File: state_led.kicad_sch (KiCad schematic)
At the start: 5 parts

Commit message: routing done
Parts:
- removed D1, D2, D3, D4, D5: White, LED_SMD:LED_0603_1608Metric, symbol Device:LED
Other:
- added sheet LED array x5 (led_x5.kicad_sch)
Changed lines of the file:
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@@
 (kicad_sch (version 20211123) (generator eeschema)
   (paper "A4")
-  (junction (at 106.68 109.855) (diameter 0) (color 0 0 0 0)
-  )
-  (junction (at 106.68 90.805) (diameter 0) (color 0 0 0 0)
-  )
-  (junction (at 106.68 103.505) (diameter 0) (color 0 0 0 0)
-  )
-  (junction (at 106.68 97.155) (diameter 0) (color 0 0 0 0)
-  )
-  (wire (pts (xy 106.68 109.855) (xy 106.68 103.505))
+  (wire (pts (xy 111.125 83.185) (xy 114.3 83.185))
     (stroke (width 0) (type default) (color 0 0 0 0))
   )
-  (wire (pts (xy 106.68 97.155) (xy 106.68 90.805))
+  (wire (pts (xy 111.125 88.9) (xy 114.3 88.9))
     (stroke (width 0) (type default) (color 0 0 0 0))
   )
-  (wire (pts (xy 106.68 90.805) (xy 106.68 84.455))
+  (wire (pts (xy 111.125 85.09) (xy 114.3 85.09))
     (stroke (width 0) (type default) (color 0 0 0 0))
   )
-  (wire (pts (xy 106.68 103.505) (xy 106.68 97.155))
+  (wire (pts (xy 111.125 81.28) (xy 114.3 81.28))
+    (stroke (width 0) (type default) (color 0 0 0 0))
+  )
+  (wire (pts (xy 111.125 86.995) (xy 114.3 86.995))
     (stroke (width 0) (type default) (color 0 0 0 0))
   )
   (hierarchical_label "STATE" (shape input) (at 114.3 76.2 180)
     (effects (font (size 1.27 1.27)) (justify right))
-  )
-  (symbol (lib_id "Device:LED") (at 110.49 97.155 180) (unit 1)
-    (in_bom yes) (on_board yes) (fields_autoplaced)
-    (property "Reference" "D3" (id 0) (at 112.0775 93.8332 0))
-    (property "Value" "White" (id 1) (at 113.7797 94.234 90)
-      (effects (font (size 1.27 1.27)) (justify right) hide)
-    )
-    (property "Footprint" "LED_SMD:LED_0603_1608Metric" (id 2) (at 110.49 97.155 0)
-      (effects (font (size 1.27 1.27)) hide)
-    )
-    (property "Datasheet" "https://datasheet.lcsc.com/lcsc/1809041711_Hubei-KENTO-Elec-C2290_C2290.pdf" (id 3) (at 110.49 97.155 0)
-      (effects (font (size 1.27 1.27)) hide)
-    )
-    (property "JLC" "C2290" (id 4) (at 110.49 97.155 90)
-      (effects (font (size 1.27 1.27)) hide)
-    )
-    (pin "1")
-    (pin "2")
-  )
-  (symbol (lib_id "Device:LED") (at 110.49 109.855 180) (unit 1)
-    (in_bom yes) (on_board yes) (fields_autoplaced)
-    (property "Reference" "D5" (id 0) (at 112.0775 106.5332 0))
-    (property "Value" "White" (id 1) (at 113.7797 106.934 90)
-      (effects (font (size 1.27 1.27)) (justify right) hide)
-    )
-    (property "Footprint" "LED_SMD:LED_0603_1608Metric" (id 2) (at 110.49 109.855 0)
-      (effects (font (size 1.27 1.27)) hide)
-    )
-    (property "Datasheet" "https://datasheet.lcsc.com/lcsc/1809041711_Hubei-KENTO-Elec-C2290_C2290.pdf" (id 3) (at 110.49 109.855 0)
-      (effects (font (size 1.27 1.27)) hide)
-    )
-    (property "JLC" "C2290" (id 4) (at 110.49 109.855 90)
-      (effects (font (size 1.27 1.27)) hide)
-    )
-    (pin "1")
-    (pin "2")
-  )
-  (symbol (lib_id "Device:LED") (at 110.49 84.455 180) (unit 1)
-    (in_bom yes) (on_board yes) (fields_autoplaced)
-    (property "Reference" "D1" (id 0) (at 112.0775 81.1332 0))
-    (property "Value" "White" (id 1) (at 113.7797 81.534 90)
-      (effects (font (size 1.27 1.27)) (justify right) hide)
-    )
-    (property "Footprint" "LED_SMD:LED_0603_1608Metric" (id 2) (at 110.49 84.455 0)
-      (effects (font (size 1.27 1.27)) hide)
-    )
-    (property "Datasheet" "https://datasheet.lcsc.com/lcsc/1809041711_Hubei-KENTO-Elec-C2290_C2290.pdf" (id 3) (at 110.49 84.455 0)
-      (effects (font (size 1.27 1.27)) hide)
-    )
-    (property "JLC" "C2290" (id 4) (at 110.49 84.455 90)
-      (effects (font (size 1.27 1.27)) hide)
-    )
-    (pin "1")
-    (pin "2")
-  )
-  (symbol (lib_id "power:VDD") (at 106.68 109.855 90) (unit 1)
-    (in_bom yes) (on_board yes) (fields_autoplaced)
-    (property "Reference" "#PWR021" (id 0) (at 110.49 109.855 0)
-      (effects (font (size 1.27 1.27)) hide)
-    )
-    (property "Value" "VDD" (id 1) (at 103.505 110.2888 90)
-      (effects (font (size 1.27 1.27)) (justify left))
-    )
-    (property "Footprint" "" (id 2) (at 106.68 109.855 0)
-      (effects (font (size 1.27 1.27)) hide)
-    )
-    (property "Datasheet" "" (id 3) (at 106.68 109.855 0)
-      (effects (font (size 1.27 1.27)) hide)
-    )
-    (pin "1")
-  )
-  (symbol (lib_id "Device:LED") (at 110.49 90.805 180) (unit 1)
-    (in_bom yes) (on_board yes) (fields_autoplaced)
-    (property "Reference" "D2" (id 0) (at 112.0775 87.4832 0))
-    (property "Value" "White" (id 1) (at 113.7797 87.884 90)
-      (effects (font (size 1.27 1.27)) (justify right) hide)
-    )
-    (property "Footprint" "LED_SMD:LED_0603_1608Metric" (id 2) (at 110.49 90.805 0)
-      (effects (font (size 1.27 1.27)) hide)
-    )
-    (property "Datasheet" "https://datasheet.lcsc.com/lcsc/1809041711_Hubei-KENTO-Elec-C2290_C2290.pdf" (id 3) (at 110.49 90.805 0)
-      (effects (font (size 1.27 1.27)) hide)
-    )
-    (property "JLC" "C2290" (id 4) (at 110.49 90.805 90)
-      (effects (font (size 1.27 1.27)) hide)
-    )
-    (pin "1")
-    (pin "2")
-  )
-  (symbol (lib_id "Device:LED") (at 110.49 103.505 180) (unit 1)
-    (in_bom yes) (on_board yes) (fields_autoplaced)
-    (property "Reference" "D4" (id 0) (at 112.0775 100.1832 0))
-    (property "Value" "White" (id 1) (at 113.7797 100.584 90)
-      (effects (font (size 1.27 1.27)) (justify right) hide)
-    )
-    (property "Footprint" "LED_SMD:LED_0603_1608Metric" (id 2) (at 110.49 103.505 0)
-      (effects (font (size 1.27 1.27)) hide)
-    )
-    (property "Datasheet" "https://datasheet.lcsc.com/lcsc/1809041711_Hubei-KENTO-Elec-C2290_C2290.pdf" (id 3) (at 110.49 103.505 0)
-      (effects (font (size 1.27 1.27)) hide)
-    )
-    (property "JLC" "C2290" (id 4) (at 110.49 103.505 90)
-      (effects (font (size 1.27 1.27)) hide)
-    )
-    (pin "1")
-    (pin "2")
   )
   (sheet (at 114.3 74.93) (size 12.7 40.005) (fields_autoplaced)
@@
       (effects (font (size 1.27 1.27)) (justify left top) hide)
     )
-    (pin "LED2" passive (at 114.3 90.805 180)
+    (pin "LED2" passive (at 114.3 83.185 180)
       (effects (font (size 1.27 1.27)) (justify left))
     )
-    (pin "LED1" passive (at 114.3 84.455 180)
+    (pin "LED1" passive (at 114.3 81.28 180)
       (effects (font (size 1.27 1.27)) (justify left))
     )
-    (pin "LED3" passive (at 114.3 97.155 180)
+    (pin "LED3" passive (at 114.3 85.09 180)
       (effects (font (size 1.27 1.27)) (justify left))
     )
@@
       (effects (font (size 1.27 1.27)) (justify left))
     )
-    (pin "LED4" passive (at 114.3 103.505 180)
+    (pin "LED4" passive (at 114.3 86.995 180)
       (effects (font (size 1.27 1.27)) (justify left))
     )
-    (pin "LED5" passive (at 114.3 109.855 180)
+    (pin "LED5" passive (at 114.3 88.9 180)
       (effects (font (size 1.27 1.27)) (justify left))
     )
   )
+  (sheet (at 93.98 80.01) (size 17.145 10.16) (fields_autoplaced)
+    (stroke (width 0.1524) (type solid) (color 0 0 0 0))
+    (fill (color 0 0 0 0.0000))
+    (property "Sheet name" "LED array x5" (id 0) (at 93.98 79.2984 0)
+      (effects (font (size 1.27 1.27)) (justify left bottom))
+    )
+    (property "Sheet file" "led_x5.kicad_sch" (id 1) (at 93.98 90.7546 0)
+      (effects (font (size 1.27 1.27)) (justify left top) hide)
+    )
+    (pin "LED3" passive (at 111.125 85.09 0)
+      (effects (font (size 1.27 1.27)) (justify right))
+    )
+    (pin "LED4" passive (at 111.125 86.995 0)
+      (effects (font (size 1.27 1.27)) (justify right))
+    )
+    (pin "LED1" passive (at 111.125 81.28 0)
+      (effects (font (size 1.27 1.27)) (justify right))
+    )
+    (pin "LED2" passive (at 111.125 83.185 0)
+      (effects (font (size 1.27 1.27)) (justify right))
+    )
+    (pin "LED5" passive (at 111.125 88.9 0)
+      (effects (font (size 1.27 1.27)) (justify right))
+    )
+  )

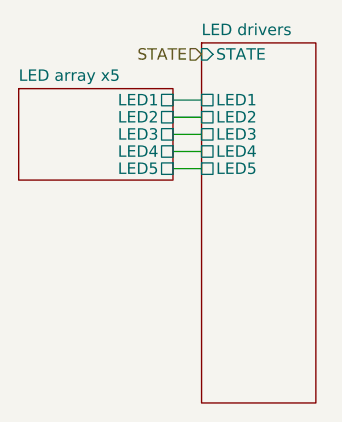
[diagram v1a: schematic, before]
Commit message: started fixing issues from V1
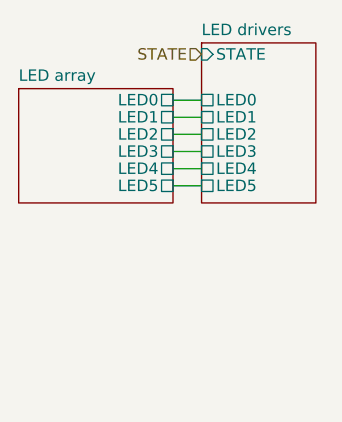
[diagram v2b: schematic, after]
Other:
- sheet LED array x5 renamed LED array
- sheet LED array ports: added LED0; removed none
- sheet LED drivers ports: added LED0; removed none
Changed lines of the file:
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@@
+    (stroke (width 0) (type default) (color 0 0 0 0))
+  )
+  (wire (pts (xy 111.125 90.805) (xy 114.3 90.805))
     (stroke (width 0) (type default) (color 0 0 0 0))
   )
@@
     (effects (font (size 1.27 1.27)) (justify right))
   )
-  (sheet (at 114.3 74.93) (size 12.7 40.005) (fields_autoplaced)
+  (sheet (at 114.3 74.93) (size 12.7 17.78) (fields_autoplaced)
     (stroke (width 0.1524) (type solid) (color 0 0 0 0))
     (fill (color 0 0 0 0.0000))
@@
       (effects (font (size 1.27 1.27)) (justify left bottom))
     )
-    (property "Sheet file" "led_drivers.kicad_sch" (id 1) (at 114.3 115.5196 0)
+    (property "Sheet file" "led_drivers.kicad_sch" (id 1) (at 114.3 93.2946 0)
       (effects (font (size 1.27 1.27)) (justify left top) hide)
     )
-    (pin "LED2" passive (at 114.3 83.185 180)
+    (pin "LED2" passive (at 114.3 85.09 180)
       (effects (font (size 1.27 1.27)) (justify left))
     )
-    (pin "LED1" passive (at 114.3 81.28 180)
+    (pin "LED1" passive (at 114.3 83.185 180)
       (effects (font (size 1.27 1.27)) (justify left))
     )
-    (pin "LED3" passive (at 114.3 85.09 180)
+    (pin "LED3" passive (at 114.3 86.995 180)
       (effects (font (size 1.27 1.27)) (justify left))
     )
@@
       (effects (font (size 1.27 1.27)) (justify left))
     )
-    (pin "LED4" passive (at 114.3 86.995 180)
+    (pin "LED4" passive (at 114.3 88.9 180)
       (effects (font (size 1.27 1.27)) (justify left))
     )
-    (pin "LED5" passive (at 114.3 88.9 180)
+    (pin "LED5" passive (at 114.3 90.805 180)
+      (effects (font (size 1.27 1.27)) (justify left))
+    )
+    (pin "LED0" passive (at 114.3 81.28 180)
       (effects (font (size 1.27 1.27)) (justify left))
     )
   )
-  (sheet (at 93.98 80.01) (size 17.145 10.16) (fields_autoplaced)
+  (sheet (at 93.98 80.01) (size 17.145 12.7) (fields_autoplaced)
     (stroke (width 0.1524) (type solid) (color 0 0 0 0))
     (fill (color 0 0 0 0.0000))
-    (property "Sheet name" "LED array x5" (id 0) (at 93.98 79.2984 0)
+    (property "Sheet name" "LED array" (id 0) (at 93.98 79.2984 0)
       (effects (font (size 1.27 1.27)) (justify left bottom))
     )
-    (property "Sheet file" "led_x5.kicad_sch" (id 1) (at 93.98 90.7546 0)
+    (property "Sheet file" "led_x5.kicad_sch" (id 1) (at 93.98 93.2946 0)
       (effects (font (size 1.27 1.27)) (justify left top) hide)
     )
-    (pin "LED3" passive (at 111.125 85.09 0)
+    (pin "LED3" passive (at 111.125 86.995 0)
       (effects (font (size 1.27 1.27)) (justify right))
     )
-    (pin "LED4" passive (at 111.125 86.995 0)
+    (pin "LED4" passive (at 111.125 88.9 0)
       (effects (font (size 1.27 1.27)) (justify right))
     )
-    (pin "LED1" passive (at 111.125 81.28 0)
+    (pin "LED1" passive (at 111.125 83.185 0)
       (effects (font (size 1.27 1.27)) (justify right))
     )
-    (pin "LED2" passive (at 111.125 83.185 0)
+    (pin "LED2" passive (at 111.125 85.09 0)
       (effects (font (size 1.27 1.27)) (justify right))
     )
-    (pin "LED5" passive (at 111.125 88.9 0)
+    (pin "LED5" passive (at 111.125 90.805 0)
       (effects (font (size 1.27 1.27)) (justify right))
     )
+    (pin "LED0" passive (at 111.125 81.28 0)
+      (effects (font (size 1.27 1.27)) (justify right))
+    )
